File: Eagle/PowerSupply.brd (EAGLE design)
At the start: 100 x 80 mm, 16 parts, among them IC1 7812T, X1 MKDSN1,5/3-5,08, X2 MKDSN1,5/2-5,08, X3 MKDSN1,5/2-5,08, X4 MKDSN1,5/2-5,08, X5 MKDSN1,5/2-5,08, X6 MKDSN1,5/3-5,08

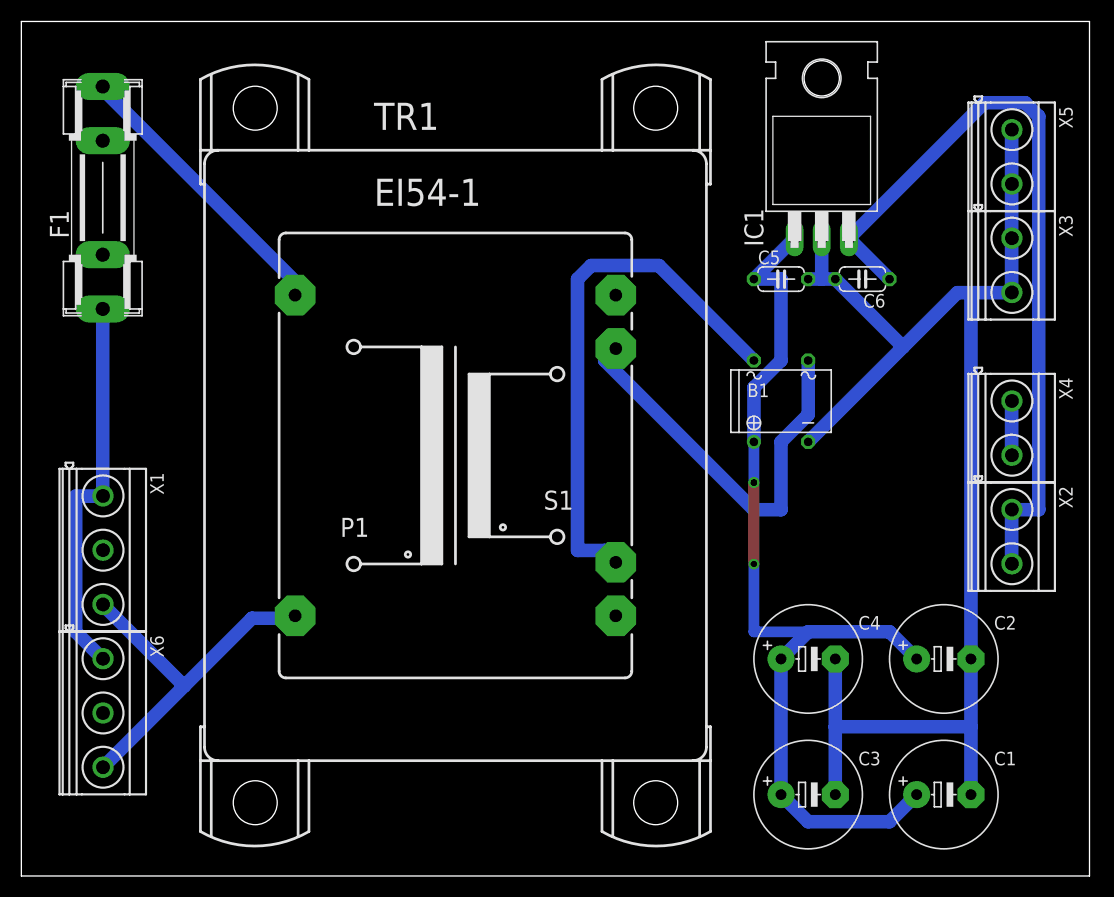
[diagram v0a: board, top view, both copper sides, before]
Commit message: - AntennaBoard: ERC errors fixed, worked on board and DRC - PowerSupply: ERC & DRC errors fixed
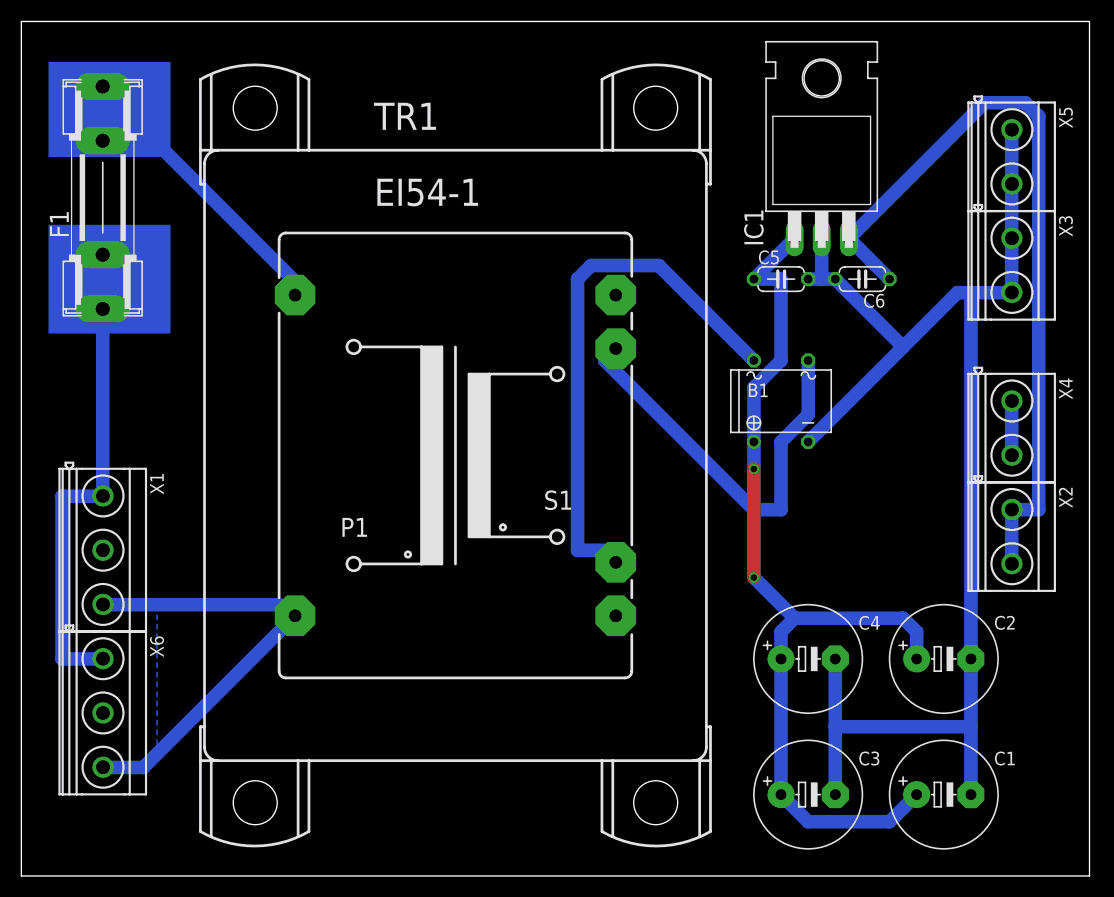
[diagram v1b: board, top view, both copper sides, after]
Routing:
- net N$8: track 34.7 -> 41.9 mm
- net N$1: track 36.4 -> 40.5 mm
- net N$6: track 89.4 -> 88.6 mm
- added copper zone on layer 16, net N$8
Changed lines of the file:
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@@
 <wire x1="100" y1="80" x2="0" y2="80" width="0" layer="20"/>
 <wire x1="0" y1="80" x2="0" y2="0" width="0" layer="20"/>
+<rectangle x1="2.54" y1="67.31" x2="13.97" y2="76.2" layer="16"/>
+<rectangle x1="2.54" y1="50.8" x2="13.97" y2="60.96" layer="16"/>
 </plain>
 <attributes>
@@
 <contactref element="X1" pad="1"/>
 <contactref element="X6" pad="1"/>
-<wire x1="5.08" y1="22.86" x2="7.62" y2="20.32" width="1.27" layer="16"/>
-<wire x1="5.08" y1="35.56" x2="5.08" y2="22.86" width="1.27" layer="16"/>
-<wire x1="7.62" y1="35.56" x2="5.08" y2="35.56" width="1.27" layer="16"/>
 <wire x1="7.62" y1="20.32" x2="7.645" y2="20.3411" width="1.27" layer="16"/>
 <wire x1="7.62" y1="35.56" x2="7.62" y2="53.086" width="1.27" layer="16"/>
 <wire x1="7.62" y1="35.56" x2="7.645" y2="35.5811" width="1.27" layer="16"/>
+<wire x1="7.62" y1="20.32" x2="3.81" y2="20.32" width="1.27" layer="16"/>
+<wire x1="3.81" y1="20.32" x2="3.81" y2="35.56" width="1.27" layer="16"/>
+<wire x1="3.81" y1="35.56" x2="7.62" y2="35.56" width="1.27" layer="16"/>
 </signal>
 <signal name="N$2">
@@
 <wire x1="7.62" y1="73.66" x2="7.62" y2="73.914" width="1.27" layer="16"/>
 <wire x1="26.67" y1="54.61" x2="25.6286" y2="54.3814" width="1.27" layer="16"/>
-</signal>
-<signal name="N$3">
-<contactref element="TR1" pad="7"/>
-<contactref element="X1" pad="3"/>
-<contactref element="X6" pad="3"/>
-<wire x1="21.59" y1="24.13" x2="15.24" y2="17.78" width="1.27" layer="16"/>
-<wire x1="15.24" y1="17.78" x2="7.62" y2="10.16" width="1.27" layer="16"/>
-<wire x1="25.4" y1="24.13" x2="21.59" y2="24.13" width="1.27" layer="16"/>
-<wire x1="7.62" y1="10.16" x2="7.645" y2="10.1811" width="1.27" layer="16"/>
-<wire x1="25.4" y1="24.13" x2="25.6286" y2="24.3586" width="1.27" layer="16"/>
-<wire x1="15.24" y1="17.78" x2="7.62" y2="25.4" width="1.27" layer="16"/>
-<wire x1="7.62" y1="25.4" x2="7.645" y2="25.4211" width="1.27" layer="16"/>
 </signal>
 <signal name="N$4">
@@
 <wire x1="73.66" y1="5.08" x2="81.28" y2="5.08" width="1.27" layer="16"/>
 <wire x1="71.12" y1="7.62" x2="73.66" y2="5.08" width="1.27" layer="16"/>
-<wire x1="68.58" y1="40.64" x2="68.58" y2="36.83" width="1.016" layer="16"/>
-<via x="68.58" y="36.83" extent="1-16" drill="0.6"/>
-<wire x1="68.58" y1="36.83" x2="68.58" y2="29.21" width="1.016" layer="1"/>
-<wire x1="81.28" y1="22.86" x2="83.82" y2="20.32" width="1.27" layer="16"/>
-<wire x1="73.66" y1="22.86" x2="81.28" y2="22.86" width="1.27" layer="16"/>
-<wire x1="71.12" y1="20.32" x2="73.66" y2="22.86" width="1.27" layer="16"/>
-<via x="68.58" y="36.83" extent="1-16" drill="0.6"/>
-<wire x1="73.66" y1="22.86" x2="68.58" y2="22.86" width="1.016" layer="16"/>
-<wire x1="68.58" y1="22.86" x2="68.58" y2="29.21" width="1.016" layer="16"/>
-<wire x1="68.58" y1="29.21" x2="68.58" y2="29.21" width="0" layer="19" extent="1-16"/>
+<wire x1="83.82" y1="20.32" x2="83.82" y2="22.86" width="1.27" layer="16"/>
+<wire x1="83.82" y1="22.86" x2="82.55" y2="24.13" width="1.27" layer="16"/>
+<wire x1="82.55" y1="24.13" x2="72.39" y2="24.13" width="1.27" layer="16"/>
+<wire x1="72.39" y1="24.13" x2="71.12" y2="22.86" width="1.27" layer="16"/>
+<wire x1="71.12" y1="22.86" x2="71.12" y2="20.32" width="1.27" layer="16"/>
+<wire x1="72.39" y1="24.13" x2="68.58" y2="27.94" width="1.27" layer="16"/>
+<via x="68.58" y="27.94" extent="1-16" drill="0.6" shape="square"/>
+<wire x1="68.58" y1="27.94" x2="68.58" y2="38.1" width="1.27" layer="1"/>
+<via x="68.58" y="38.1" extent="1-16" drill="0.6" shape="square"/>
+<wire x1="68.58" y1="38.1" x2="68.58" y2="40.64" width="1.27" layer="16"/>
 </signal>
 <signal name="+12V">
@@
 </signal>
 <signal name="N$8">
-<via x="68.58" y="29.21" extent="1-16" drill="0.6"/>
+<polygon width="1.27" layer="16">
+<vertex x="12.7" y="25.4"/>
+<vertex x="12.7" y="11.43"/>
+<vertex x="25.4" y="24.13"/>
+<vertex x="24.13" y="25.4"/>
+</polygon>
+<contactref element="TR1" pad="7"/>
+<contactref element="X1" pad="3"/>
+<contactref element="X6" pad="3"/>
+<wire x1="7.645" y1="25.4211" x2="7.6661" y2="25.4" width="1.27" layer="16"/>
+<wire x1="7.6661" y1="25.4" x2="24.13" y2="25.4" width="1.27" layer="16"/>
+<wire x1="24.13" y1="25.4" x2="25.4" y2="24.13" width="1.27" layer="16"/>
+<wire x1="25.4" y1="24.13" x2="11.43" y2="10.16" width="1.27" layer="16"/>
+<wire x1="11.43" y1="10.16" x2="7.62" y2="10.16" width="1.27" layer="16"/>
+<wire x1="25.4" y1="24.13" x2="25.6286" y2="24.3586" width="0" layer="19" extent="16-16"/>
+<wire x1="7.645" y1="10.1811" x2="7.62" y2="10.16" width="0" layer="19" extent="16-16"/>
 </signal>
 </signals>

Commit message: - fixed some error, re-routing done
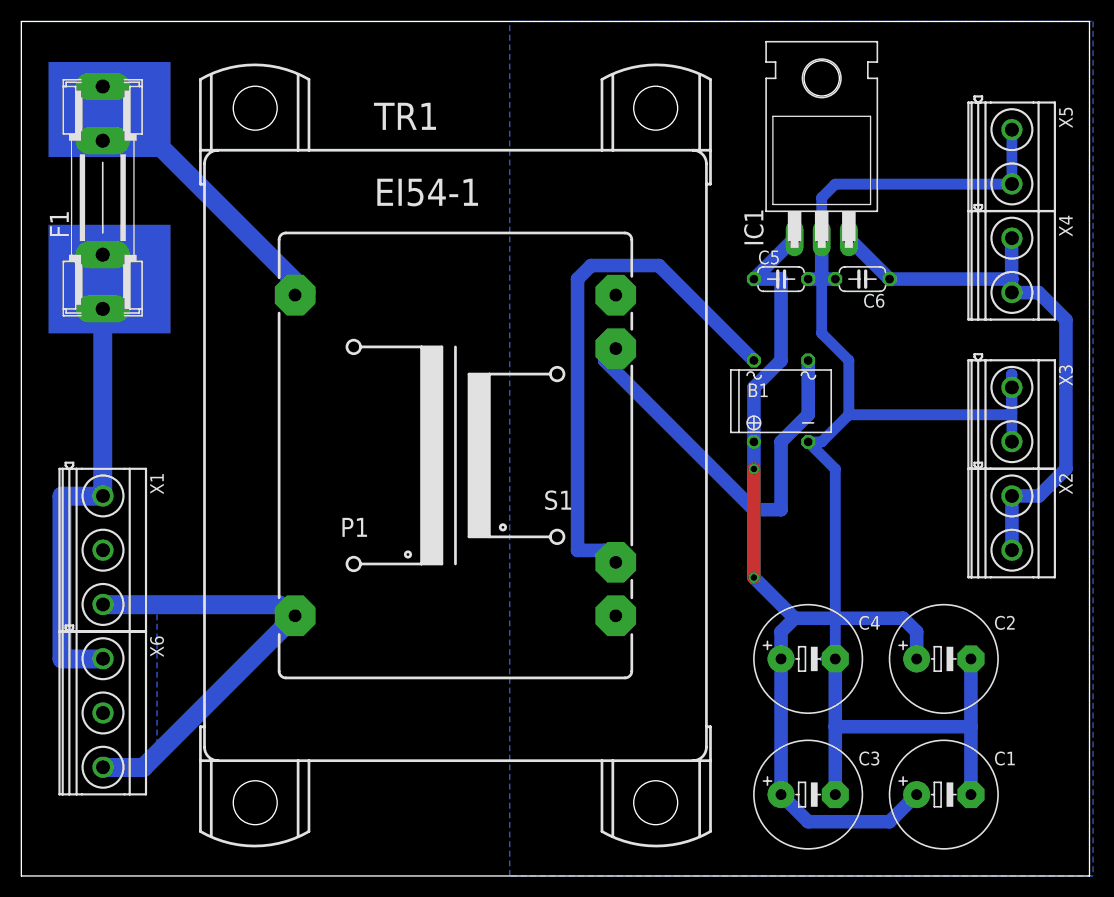
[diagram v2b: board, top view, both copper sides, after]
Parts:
- moved X4 15.2 mm to (92.7, 57.1)
- moved X3 14.0 mm to (92.7, 43.2)
- moved X2 1.27 mm to (92.7, 33.0)
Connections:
- removed net N$7: X4.1, X4.2
- net +12V: now also X4.1, X4.2
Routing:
- net +12V: track 73.5 -> 53.2 mm
- net 0V: track 127.9 -> 142.7 mm
- net N$7: track 5.15 -> 0.00 mm
- added copper zone on layer 16, net N$3
